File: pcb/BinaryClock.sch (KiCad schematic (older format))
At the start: 20 parts, among them CON1 AVR-ISP-6, CON2 BARREL_JACK, U1 MC33269, U2 DS3231, U3 clock_header, U4 clock_header, U5 clock_header, U6 ATMEGA328-AU, Y1 16MHz

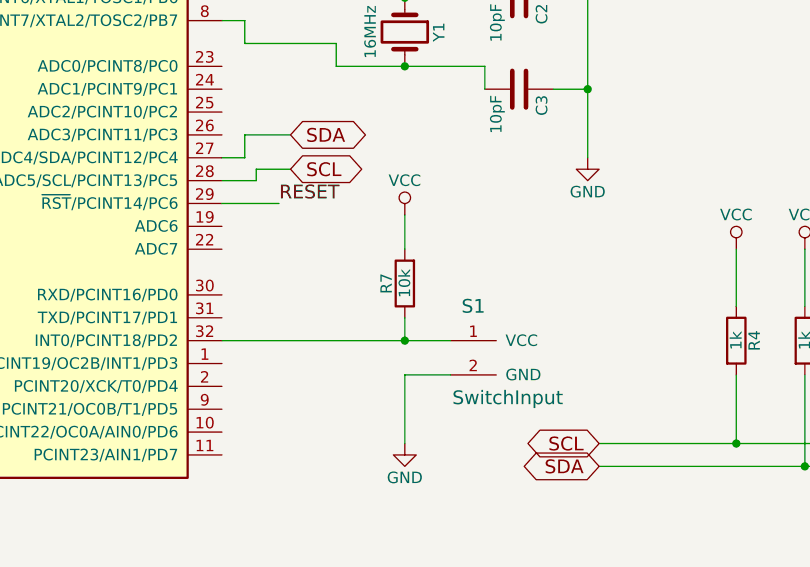
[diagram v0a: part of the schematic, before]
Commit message: Added on-board pullup resistor for external on/off switch
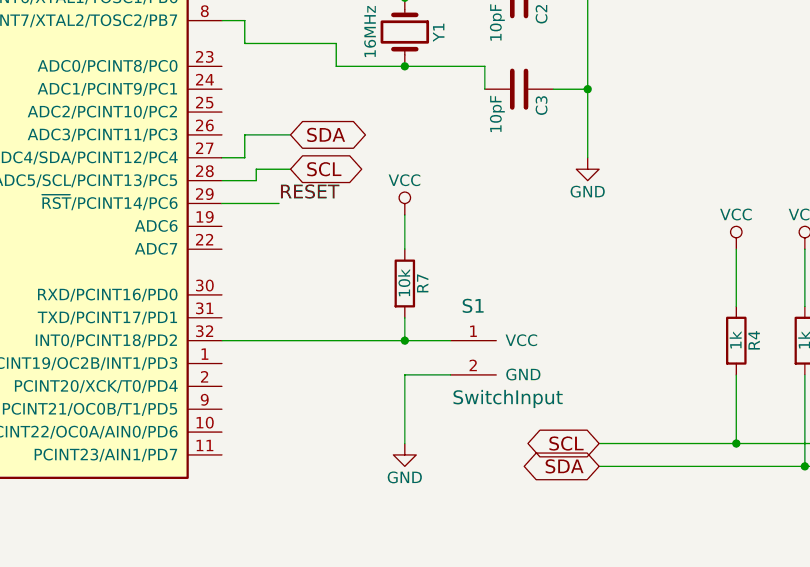
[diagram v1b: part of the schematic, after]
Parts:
- R7: footprint (none) -> Resistors_SMD:R_0805
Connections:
- net VCC: now also R7.1; no longer R7.2
- net at S1.1 (VCC), U6.32 (INT0/PCINT18/PD2): now also R7.2; no longer R7.1
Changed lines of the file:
@@
 VIN
-$Comp
-L R R7
-U 1 1 5929A12D
-P 7100 4100
-F 0 "R7" V 7180 4100 50  0000 C CNN
-F 1 "10k" V 7100 4100 50  0000 C CNN
-F 2 "" V 7030 4100 50  0000 C CNN
-F 3 "" H 7100 4100 50  0000 C CNN
-	1    7100 4100
-	-1   0    0    1
-$EndComp
 $Comp
 L GND #PWR015
@@
 	7100 4250 7100 4350
 Connection ~ 7100 4350
+$Comp
+L R R7
+U 1 1 592A0615
+P 7100 4100
+F 0 "R7" V 7180 4100 50  0000 C CNN
+F 1 "10k" V 7100 4100 50  0000 C CNN
+F 2 "Resistors_SMD:R_0805" V 7030 4100 50  0001 C CNN
+F 3 "" H 7100 4100 50  0000 C CNN
+	1    7100 4100
+	1    0    0    -1
+$EndComp
 $EndSCHEMATC
